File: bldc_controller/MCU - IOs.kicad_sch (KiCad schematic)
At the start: 7 parts, among them U1 STM32G474RET3

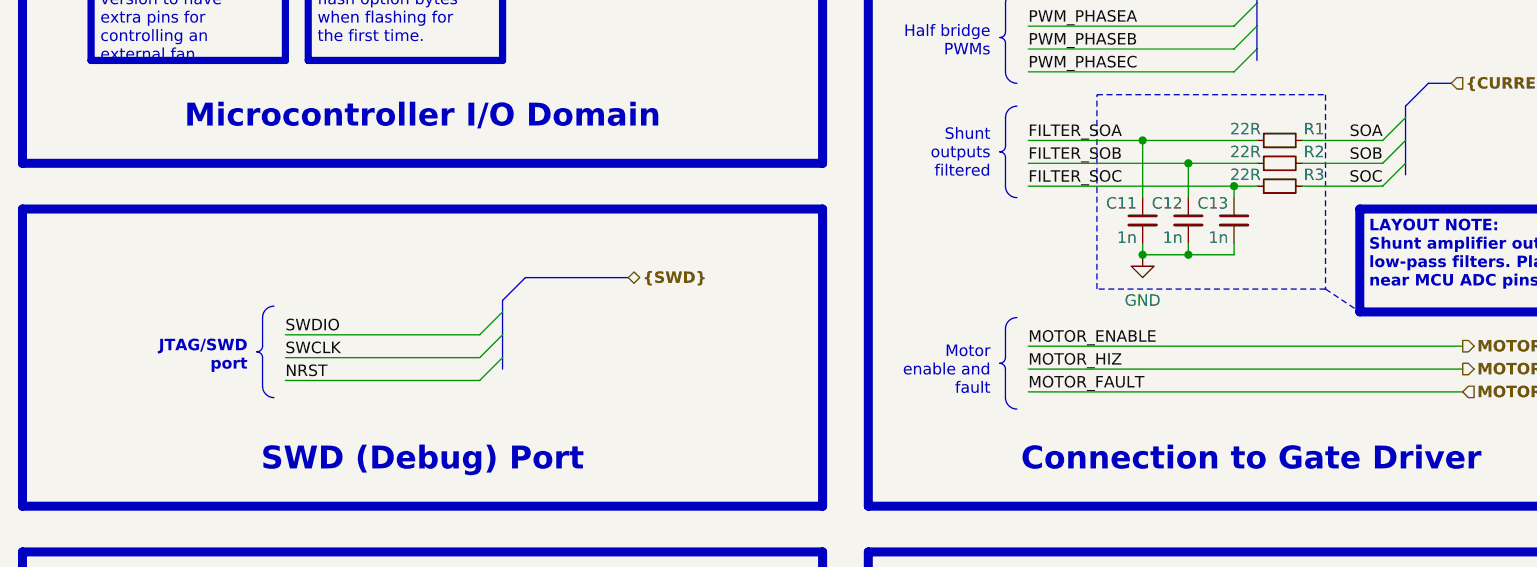
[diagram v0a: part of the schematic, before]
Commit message: schematic is complete. Replaced 5V buck and added pi filters.
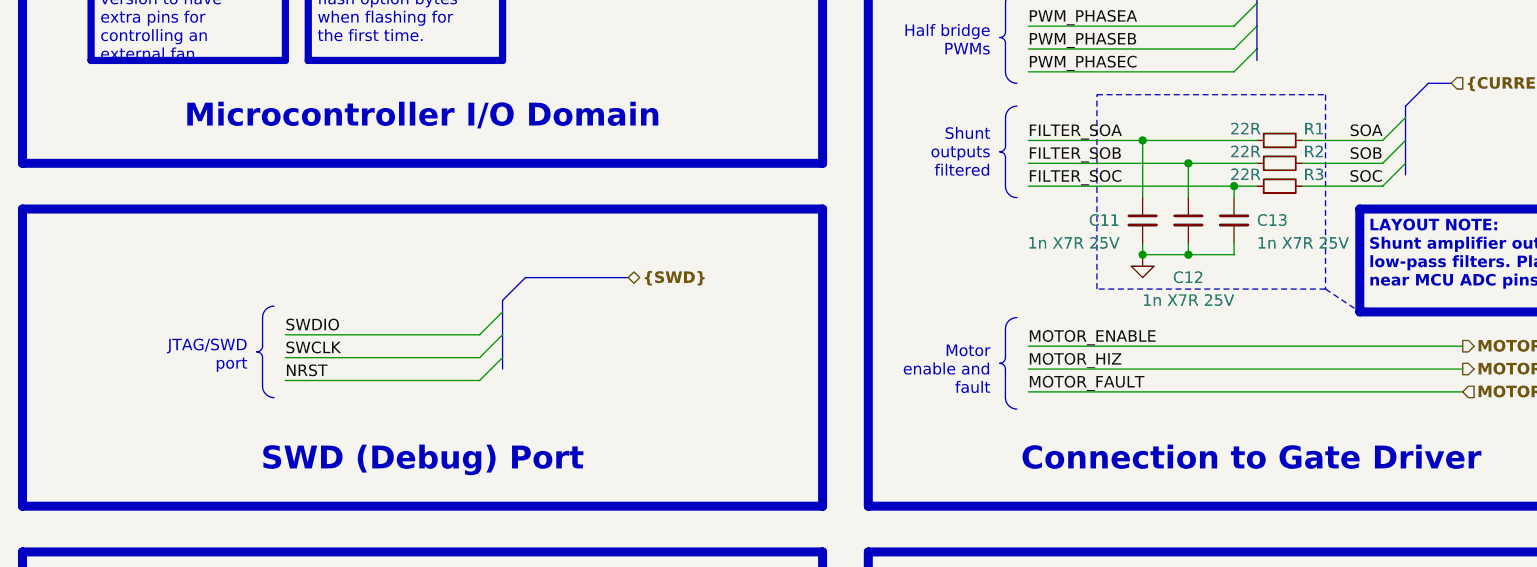
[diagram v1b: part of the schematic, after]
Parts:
- C11, C12, C13: value 1n -> 1n X7R 25V
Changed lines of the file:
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@@
     (stroke (width -0.0001) (type default))
     (fill (type none))
-    (effects (font (size 1.27 1.27)) (justify right top))
+    (effects (font (size 1.27 1.27) (color 0 0 0 1)) (justify right top))
   )
   (text_box "DESIGN NOTE:\nPC13 is used instead of PC12 for DRV_MOSI (bitbang SPI) to be compatible with moteus FW."
@@
     (stroke (width -0.0001) (type default))
     (fill (type none))
-    (effects (font (size 1.27 1.27)) (justify right top))
+    (effects (font (size 1.27 1.27) (color 0 0 0 1)) (justify right top))
   )
   (text_box "[${#}] ${TITLE}"
@@
     (stroke (width -0.0001) (type default))
     (fill (type none))
-    (effects (font (size 1.27 1.27)) (justify right top))
+    (effects (font (size 1.27 1.27) (color 0 0 0 1)) (justify right top))
   )
   (text_box "User LEDs"
@@
     (stroke (width -0.0001) (type default))
     (fill (type none))
-    (effects (font (size 1.27 1.27)) (justify right top))
+    (effects (font (size 1.27 1.27) (color 0 0 0 1)) (justify right top))
   )
   (text_box "DESIGN NOTE:\nDo not forget to flash option bytes when flashing for the first time."
@@
     (stroke (width -0.0001) (type default))
     (fill (type none))
-    (effects (font (size 1.27 1.27)) (justify right top))
+    (effects (font (size 1.27 1.27) (color 0 0 0 1)) (justify right top))
   )
   (text_box "Microcontroller I/O Domain"
@@
     (stroke (width -0.0001) (type default))
     (fill (type none))
-    (effects (font (size 1.27 1.27)) (justify right top))
+    (effects (font (size 1.27 1.27) (color 0 0 0 1)) (justify right top))
   )
   (text_box "DESIGN NOTE:\nReferences:"
@@
     (stroke (width -0.0001) (type default))
     (fill (type none))
-    (effects (font (size 1.27 1.27) (thickness 0.254) bold) (justify right top))
+    (effects (font (size 1.27 1.27) (color 0 0 0 1)) (justify right top))
   )
   (text_box "Auxiliary port 1"
@@
     (stroke (width -0.0001) (type default))
     (fill (type none))
-    (effects (font (size 1.27 1.27)) (justify right top))
+    (effects (font (size 1.27 1.27) (color 0 0 0 1)) (justify right top))
   )
   (text_box "SPI for DRV config"
@@
     (stroke (width -0.0001) (type default))
     (fill (type none))
-    (effects (font (size 1.27 1.27)) (justify right top))
+    (effects (font (size 1.27 1.27) (color 0 0 0 1)) (justify right top))
   )
   (text "Flexible I/O worked examples" (at 292.1 106.68 0)
@@
     )
     (property "Value" "GND" (at 193.04 182.88 0)
-      (effects (font (size 1.27 1.27)))
+      (effects (font (size 1.27 1.27)) hide)
     )
     (property "Footprint" "" (at 193.04 177.8 0)
@@
   (symbol (lib_id "Device:C_Small") (at 193.04 173.99 0) (mirror y) (unit 1)
     (in_bom yes) (on_board yes) (dnp no)
-    (property "Reference" "C11" (at 192.405 172.085 0)
+    (property "Reference" "C11" (at 190.5 173.99 0)
       (effects (font (size 1.27 1.27)) (justify left))
     )
-    (property "Value" "1n" (at 192.405 175.895 0)
+    (property "Value" "1n X7R 25V" (at 190.5 176.53 0)
       (effects (font (size 1.27 1.27)) (justify left))
     )
@@
   (symbol (lib_id "Device:C_Small") (at 198.12 173.99 0) (mirror y) (unit 1)
     (in_bom yes) (on_board yes) (dnp no)
-    (property "Reference" "C12" (at 197.485 172.085 0)
-      (effects (font (size 1.27 1.27)) (justify left))
-    )
-    (property "Value" "1n" (at 197.485 175.895 0)
-      (effects (font (size 1.27 1.27)) (justify left))
+    (property "Reference" "C12" (at 198.12 180.34 0)
+      (effects (font (size 1.27 1.27)))
+    )
+    (property "Value" "1n X7R 25V" (at 198.12 182.88 0)
+      (effects (font (size 1.27 1.27)))
     )
     (property "Footprint" "0_capacitor_smd:C_0402_1005_DensityHigh" (at 198.12 173.99 0)
@@
   (symbol (lib_id "Device:C_Small") (at 203.2 173.99 0) (mirror y) (unit 1)
     (in_bom yes) (on_board yes) (dnp no)
-    (property "Reference" "C13" (at 202.565 172.085 0)
-      (effects (font (size 1.27 1.27)) (justify left))
-    )
-    (property "Value" "1n" (at 202.565 175.895 0)
-      (effects (font (size 1.27 1.27)) (justify left))
+    (property "Reference" "C13" (at 205.74 173.99 0)
+      (effects (font (size 1.27 1.27)) (justify right))
+    )
+    (property "Value" "1n X7R 25V" (at 205.74 176.53 0)
+      (effects (font (size 1.27 1.27)) (justify right))
     )
     (property "Footprint" "0_capacitor_smd:C_0402_1005_DensityHigh" (at 203.2 173.99 0)

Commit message: added assembly files
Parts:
- R1, R2, R3: value 22R -> 22R 1%
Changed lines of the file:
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@@
       (effects (font (size 1.27 1.27)))
     )
-    (property "Value" "22R" (at 204.47 163.83 90)
+    (property "Value" "22R 1%" (at 203.2 163.83 90)
       (effects (font (size 1.27 1.27)))
     )
@@
       (effects (font (size 1.27 1.27)))
     )
-    (property "Value" "22R" (at 204.47 166.37 90)
+    (property "Value" "22R 1%" (at 203.2 166.37 90)
       (effects (font (size 1.27 1.27)))
     )
@@
       (effects (font (size 1.27 1.27)))
     )
-    (property "Value" "22R" (at 204.47 168.91 90)
+    (property "Value" "22R 1%" (at 203.2 168.91 90)
       (effects (font (size 1.27 1.27)))
     )
